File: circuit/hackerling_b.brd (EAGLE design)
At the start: 82.5 x 67.4 mm, 45 parts, among them IC1 MCP23017SP, IC2 MCP2300X/P, IC3 MIC5219BM5, SW2 SWITCH_B13EH, U1 MMA8452Q, U2 LCD_16X2, U3 ARDUINOR3-BPLACE, U4 ACCELEROMETER, U5 PCA9306, U6 ACCELEROMETER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

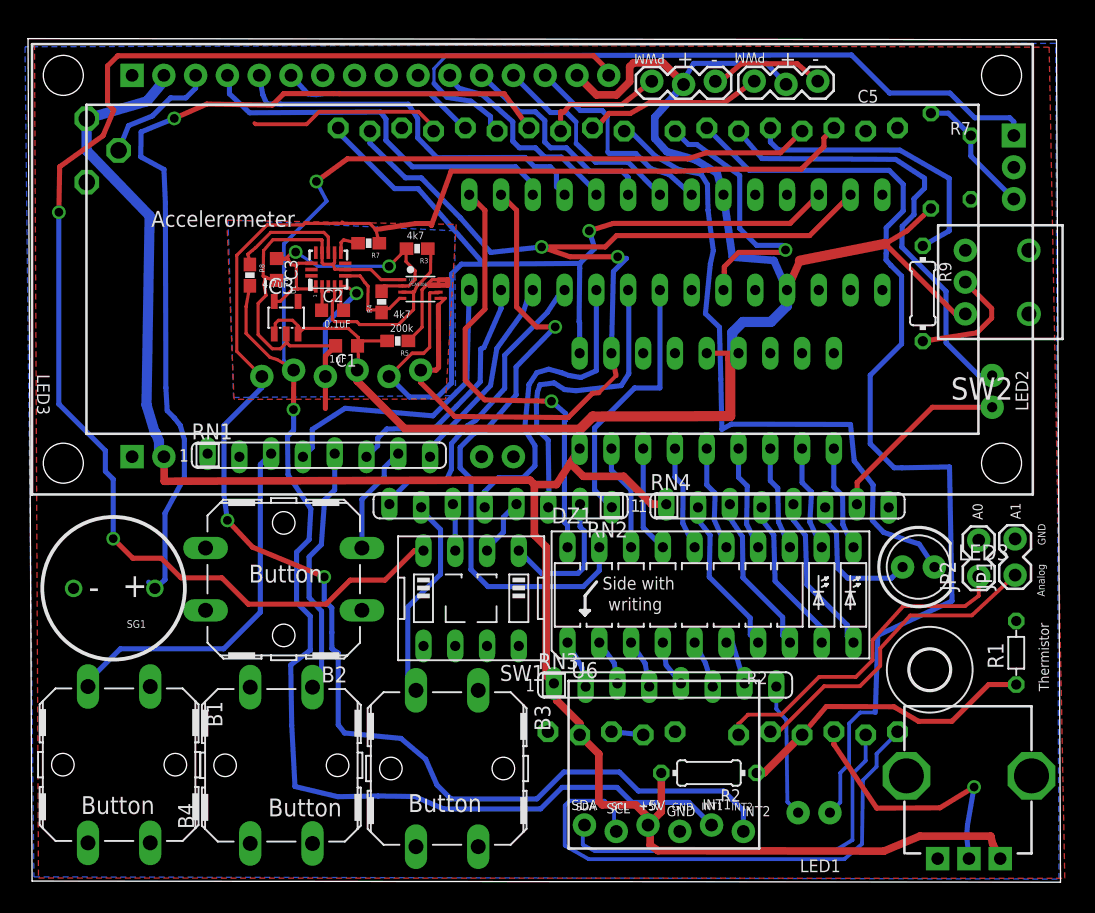
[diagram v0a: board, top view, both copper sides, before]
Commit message: made silkscreen and some cosmetic changes
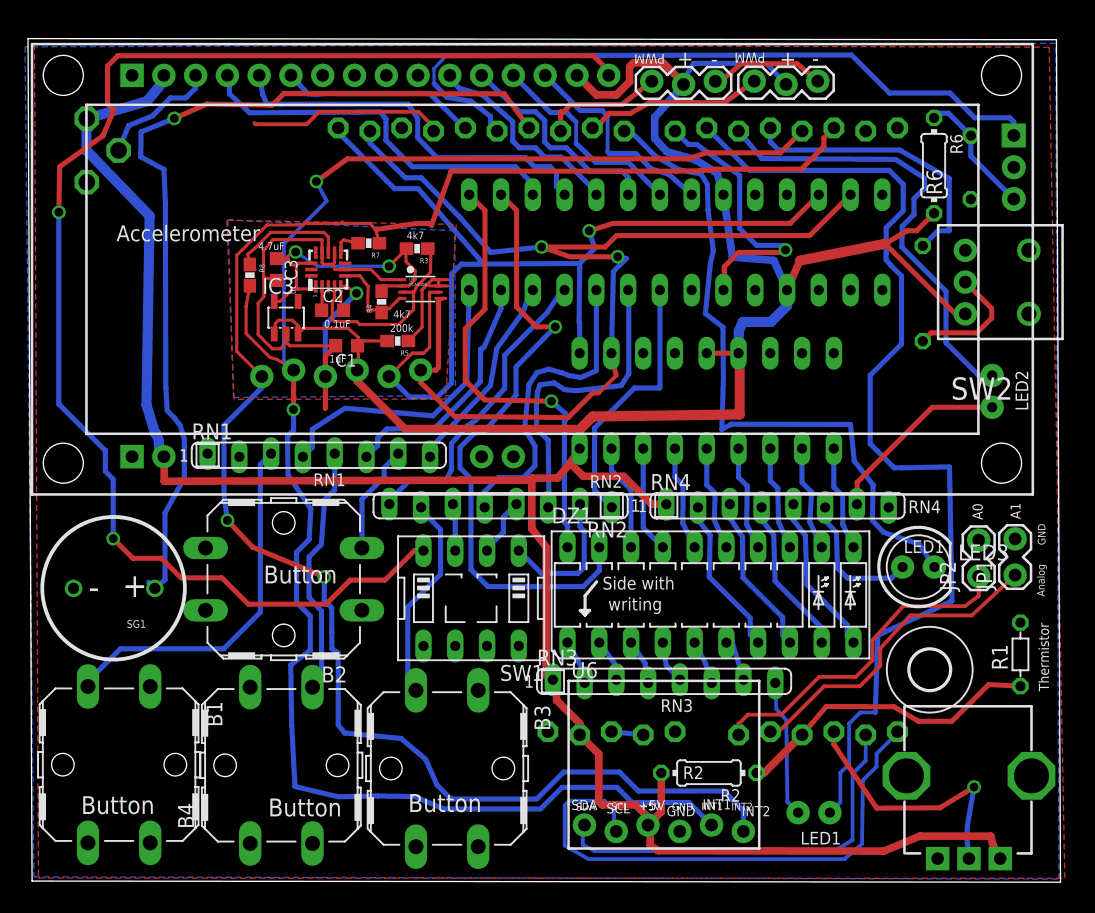
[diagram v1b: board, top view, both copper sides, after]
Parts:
- moved R6 0.46 mm to (72.2, 57.2), flipped to the top
- moved R1 0.36 mm to (79.1, 18.2)
- moved RN3 0.30 mm to (50.6, 16.0)
- flipped R9 to the bottom
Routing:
- net N$5: track 10.1 -> 9.38 mm
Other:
- board text added: "1"
- board text added: "1.2"
- board text added: "10"
- board text added: "11"
- board text added: "12"
- board text added: "13"
- board text added: "14"
- board text added: "15"
- board text added: "16"
- board text added: "17"
- board text added: "19 & 21"
- board text added: "2"
- board text added: "20"
- board text added: "22"
- board text added: "23"
- board text added: "24"
- board text added: "25"
- board text added: "26"
- board text added: "27"
- board text added: "3"
- board text added: "4"
- board text added: "5"
- board text added: "6"
- board text added: "7"
- board text added: "8"
- board text added: "9"
- board text added: "Bussed array"
- board text added: "Here"
- board text added: "Initials"
- board text added: "Install Arduino headers, pointing down."
- board text added: "LEDs"
- board text added: "Potentiometer"
- board text added: "Put Your"
- board text added: "R9"
- board text added: "RN1"
- board text added: "RN2"
- board text added: "RN3"
- board text added: "RN4"
- board text added: "like this"
- board text added: "pointing this way"
- board text removed: "1.1"
- board text removed: "16:"
- board text removed: "18,19,20:"
- board text removed: "8:"
- board text removed: "C5"
- board text removed: "Install resistor arrays"
- board text removed: "LED3"
- board text removed: "Other"
- board text removed: "R7"
- board text removed: "See"
- board text removed: "Side"
- board text removed: "Step"
- board text removed: "Step 0:"
- board text removed: "Step 10:"
- board text removed: "Step 11:"
- board text removed: "Step 12:"
- board text removed: "Step 13:"
- board text removed: "Step 14:"
- board text removed: "Step 15"
- board text removed: "Step 17:"
- board text removed: "Step 1:"
- board text removed: "Step 20:"
- board text removed: "Step 22:"
- board text removed: "Step 2:"
- board text removed: "Step 3: Install Arduino headers, pointing down."
- board text removed: "Step 4:"
- board text removed: "Step 5"
- board text removed: "Step 6"
- board text removed: "Step 7:"
- board text removed: "Step 9:"
- board text removed: "pointing down"
- board text removed: "potentiometer"

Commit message: changes made for version 1.2. ordered boards.
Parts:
- added C5: (no value), rcl:E5-4
- added U$2: HS-LOGOSMALL, hackerscouts:HS-LOGO-SM
- C4: device rcl:C050-050X075 -> hackerscouts:CAP_050X075
- moved LED1 1.39 mm to (61.3, 4.91)
- moved C1 0.92 mm to (24.3, 42.9)
- moved R2 0.82 mm to (54.0, 7.88)
- moved U7 0.73 mm to (75.5, 7.66)
- moved R6 0.49 mm to (72.6, 57.1)
- moved IR1 0.43 mm to (79.0, 57.1)
- moved RN3 0.22 mm to (50.4, 16.1)
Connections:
- net DIP1 renamed DIP4
- net DIPR1 renamed DIPR4
- net 3.3V: now also U1.15, U1.16, U1.7
- net DIP2: now also RN2.6, SW1.3; no longer RN2.4, SW1.2
- net DIP3: now also RN2.4, SW1.2; no longer RN2.6, SW1.3
- net DIPR2: now also IC1.24, RN2.5; no longer IC1.23, RN2.3
- net DIPR3: now also IC1.23, RN2.3; no longer IC1.24, RN2.5
- net GND: now also C5.-, U1.8; no longer IC1.16, IC2.4, U1.7
- net N$26: now also C5.+
- net VCC: now also IC1.16, IC2.4
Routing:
- net GND: track 75.1 -> 86.9 mm
- net N$26: track 26.8 -> 38.1 mm
- net 3.3V: track 26.6 -> 22.9 mm, vias 2 -> 0
- net DIPR4: track 21.3 -> 24.5 mm
- net N$32: track 11.0 -> 14.1 mm
- net IR_OUT2: track 36.4 -> 33.9 mm
- net BARGRAPH1: track 49.6 -> 47.5 mm
- net IR_OUT1: track 81.2 -> 79.1 mm
- net TEMP: track 24.9 -> 26.5 mm
- net IR_IN: track 58.1 -> 59.5 mm
- net A_INT2: track 138.9 -> 137.6 mm
- net DIP3: track 3.79 -> 4.69 mm
- net DIP2: track 4.69 -> 3.79 mm
- net N$15: track 72.7 -> 71.9 mm
- net SDA: track 88.8 -> 87.9 mm
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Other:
- board size 82.5 x 67.4 mm -> 83 x 67.8 mm
- board text added: "+3V"
- board text added: "28"
- board text added: "6mm away"
- board text added: "Before installing LCD Run all test programs"
- board text added: "GG"
- board text added: "Install Arduino headers on the other side"
- board text added: "LCD"
- board text added: "LED3"
- board text added: "Vin"
- board text removed: "1/4 inch away"
- board text removed: "Install Arduino headers, pointing down."

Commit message: adding version 1.3 schematics
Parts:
- removed JP1, JP2: (no value), SparkFun:1X02_LOCK
- removed SERVO2: (no value), SparkFun:1X03_LOCK
- removed U$2: HS-LOGOSMALL, hackerscouts:HS-LOGO-SM
- added HACKERSCOUTSLOGO: HS-LOGO, hackerscouts:HS-LOGO-SM-NOTEXT
- added JP3: (no value), SparkFun:1X02_LOCK
- added SERVO: (no value), SparkFun:1X03_LOCK
- added U$1: M04X2, SparkFun:2X4
- SERVO1: value (none) -> SERVO
- moved C5 24.8 mm to (41.1, 5.05)
- moved R1 18.7 mm to (63.7, 7.53), turned to 0 degrees
- moved SERVO1 1.73 mm to (59.4, 64.5)
- moved LED3 0.68 mm to (70.4, 25.5), turned to 45 degrees
- moved C1 0.51 mm to (24.3, 43.4)
- moved C2 0.51 mm to (24.1, 46.2)
- moved IC2 0.51 mm to (54.0, 38.9)
- moved IC3 0.51 mm to (20.4, 45.6)
- moved IR1 0.51 mm to (79.0, 57.6)
- moved LED2 0.51 mm to (76.8, 39.7)
- moved R4 0.51 mm to (28.0, 46.9)
- moved R5 0.51 mm to (29.3, 43.7)
- moved R6 0.51 mm to (72.6, 57.6)
- moved R7 0.51 mm to (27.0, 51.5)
- moved R8 0.51 mm to (17.5, 49.0)
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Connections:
- new net RX: JP3.2, U3.D0
- new net TX: JP3.1, U3.D1
- net GND: now also SERVO.3, U$1.5, U$1.6; no longer JP1.2, JP2.2, SERVO2.3
- net N$24: now also U$1.4; no longer JP1.1
- net N$26: now also U$1.3; no longer JP2.1
- net SVO1: now also U$1.7
- net SVO2: now also SERVO.1, U$1.8; no longer SERVO2.1
- net TEMP: now also U$1.1
- net VCC: now also SERVO.2, U$1.2; no longer SERVO2.2
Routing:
- net SVO2: track 10.1 -> 85.9 mm, vias 0 -> 1
- net SVO1: track 15.2 -> 72.8 mm, vias 0 -> 2
- net VCC: track 284.6 -> 308.8 mm, vias 0 -> 1
- net N$26: track 38.1 -> 49.2 mm
- net SCL1: track 44.4 -> 33.4 mm
- net IR_OUT2: track 33.9 -> 40.9 mm
- net RX: track 0.00 -> 5.51 mm
- net TX: track 0.00 -> 5.47 mm
- net A_INT2: track 137.6 -> 143.0 mm
- net TEMP: track 26.5 -> 31.8 mm
- net GND: track 86.9 -> 91.9 mm
- net IR_OUT1: track 79.1 -> 76.3 mm
- net N$32: track 14.1 -> 11.4 mm
- net SWITCHR: track 22.7 -> 20.0 mm
- net N$10: track 31.2 -> 32.5 mm
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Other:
- board size 83 x 67.8 mm -> 83.1 x 67.4 mm
- board text added: "1.3"
- board text added: "19 & 20"
- board text added: "500"
- board text added: "Hsync"
- board text added: "IC3"
- board text added: "Place MCP23008 here."
- board text added: "Put Your Initials Here"
- board text added: "RX"
- board text added: "S1"
- board text added: "S2"
- board text added: "TX"
- board text added: "U1"
- board text added: "U5"
- board text added: "VGA"
- board text added: "Vsync"
- board text added: "arrow goes here"
- board text added: "blue"
- board text added: "circuit.hackersource.net"
- board text added: "gnd"
- board text added: "grn"
- board text added: "power"
- board text added: "red"
- board text added: "www.hackersource.net"
- board text removed: "1.2"
- board text removed: "19 & 21"
- board text removed: "Bussed array"
- board text removed: "Here"
- board text removed: "Initials"
- board text removed: "Install 4 buttons"
- board text removed: "Place MCP2300 here."
- board text removed: "Put Your"
- board text removed: "arrow"
- board text removed: "circuit.hacker-scouts.org"
- board text removed: "goes"
- board text removed: "www.hacker-scouts.org"
